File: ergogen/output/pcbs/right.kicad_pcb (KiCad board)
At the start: 2 copper layers, 144.4 x 121 mm, 69 parts

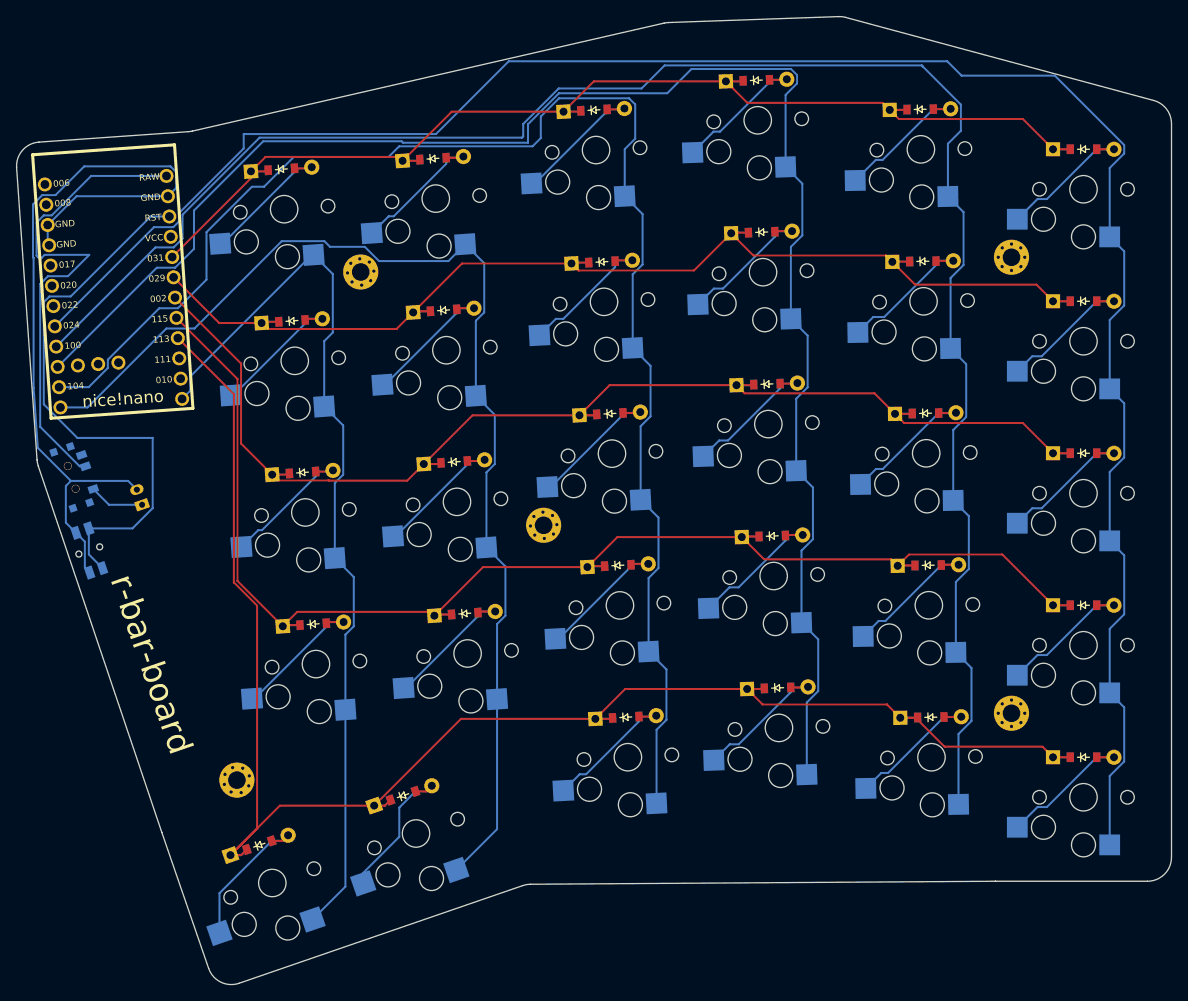
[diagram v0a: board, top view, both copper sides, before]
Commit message: Update keymap
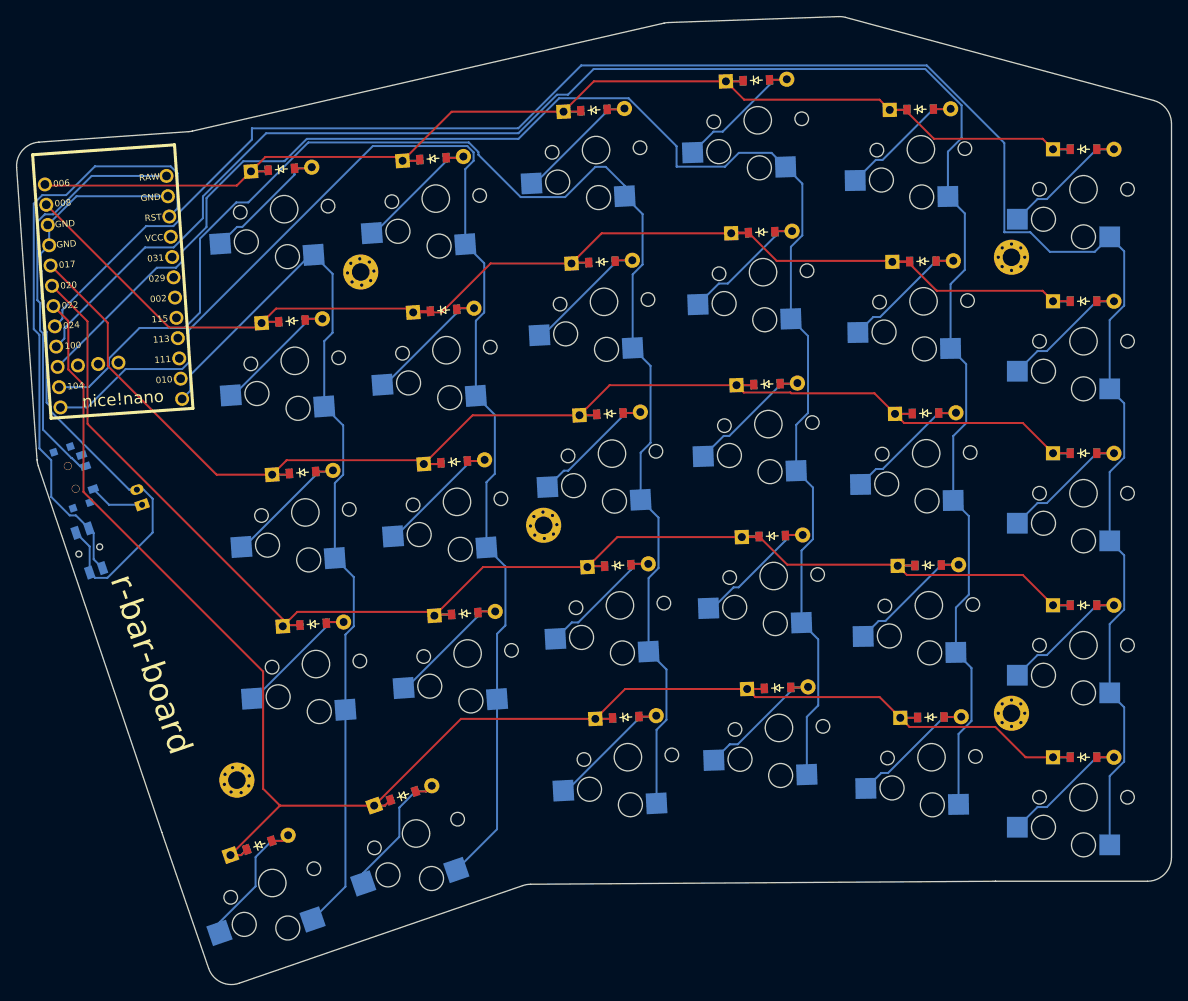
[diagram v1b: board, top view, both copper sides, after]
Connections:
- D1 pad 1: P113 -> P022
- D10 pad 1: P031 -> P006
- D11 pad 1: P113 -> P022
- D12 pad 1: P115 -> P020
- D13 pad 1: P002 -> P017
- D14 pad 1: P029 -> P008
- D15 pad 1: P031 -> P006
- D16 pad 1: P113 -> P022
- D17 pad 1: P115 -> P020
- D18 pad 1: P002 -> P017
- D19 pad 1: P029 -> P008
- D2 pad 1: P115 -> P020
- D20 pad 1: P031 -> P006
- D21 pad 1: P115 -> P020
- D22 pad 1: P002 -> P017
- D23 pad 1: P029 -> P008
- D24 pad 1: P031 -> P006
- D25 pad 1: P115 -> P020
- D26 pad 1: P002 -> P017
- D27 pad 1: P029 -> P008
- D28 pad 1: P031 -> P006
- D29 pad 1: P113 -> P022
- D3 pad 1: P002 -> P017
- D30 pad 1: P113 -> P022
- D4 pad 1: P029 -> P008
- D5 pad 1: P031 -> P006
- D6 pad 1: P113 -> P022
- D7 pad 1: P115 -> P020
- D8 pad 1: P002 -> P017
- D9 pad 1: P029 -> P008
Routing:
- net P022: track 0.00 -> 215.9 mm
- net P113: track 211.8 -> 0.00 mm
- net P020: track 0.00 -> 185.7 mm
- net P115: track 176.4 -> 0.00 mm
- net P017: track 0.00 -> 174.2 mm
- net P008: track 0.00 -> 167.3 mm
- net P006: track 0.00 -> 161.7 mm
- net P002: track 159.9 -> 0.00 mm
- net P031: track 149.9 -> 0.00 mm
- net P029: track 148.1 -> 0.00 mm
- net GND: track 100.7 -> 78.5 mm
- net P106: track 145.7 -> 164.4 mm
- net RAW: track 62.9 -> 52.0 mm
- net P011: track 206.3 -> 196.1 mm
- net P104: track 186.6 -> 177.9 mm
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
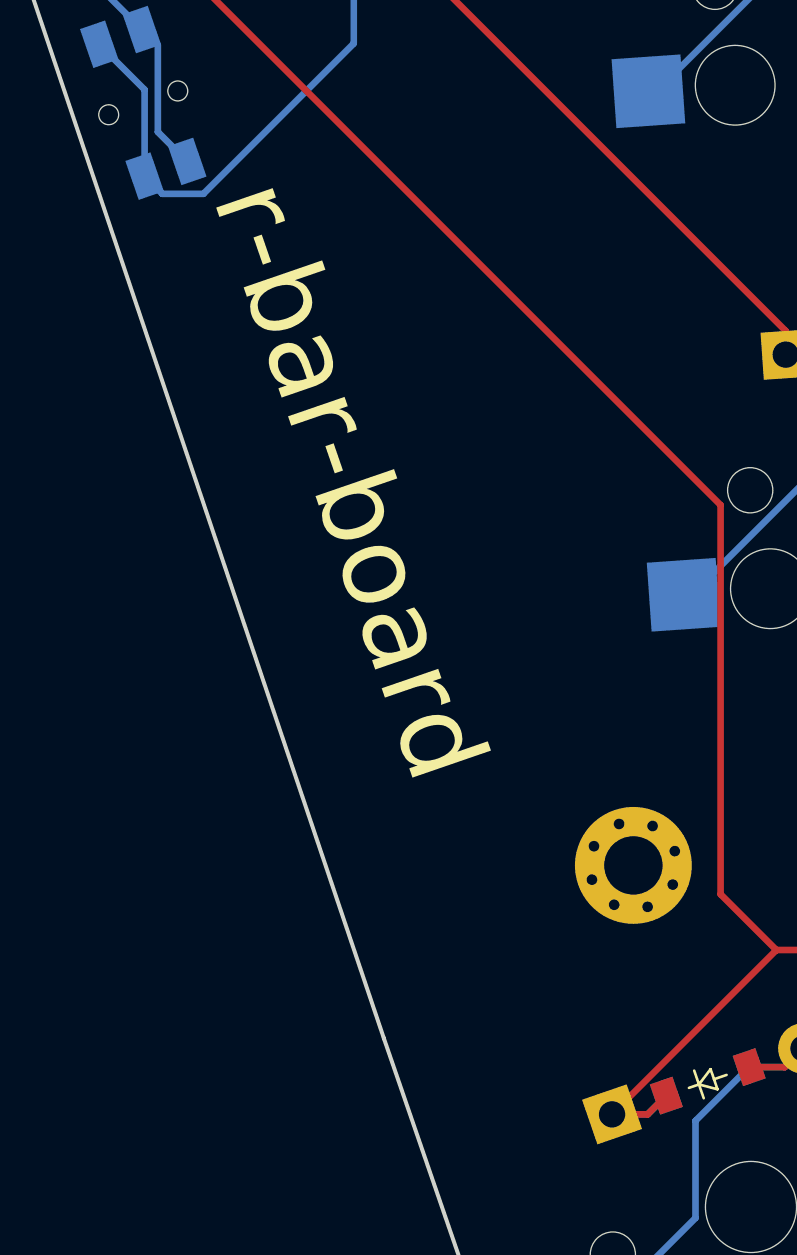
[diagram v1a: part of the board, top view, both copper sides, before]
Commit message: rename with underscores
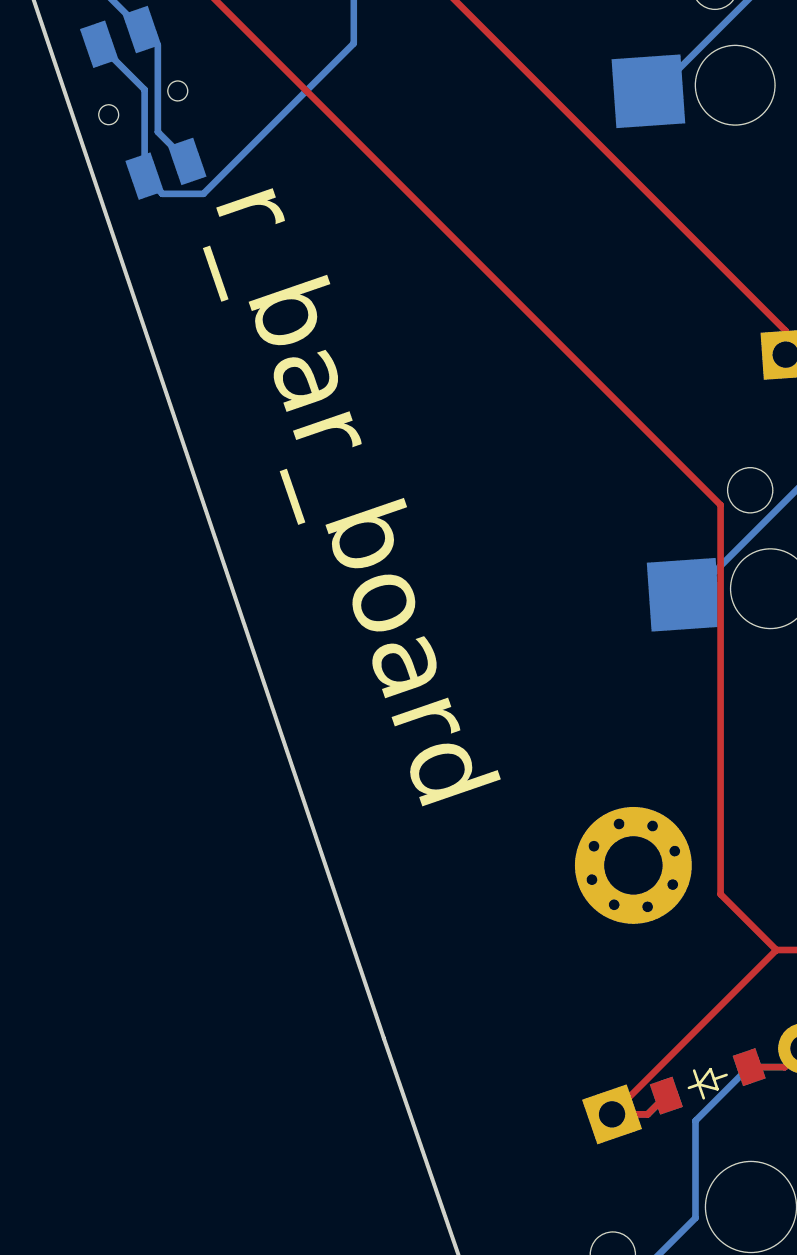
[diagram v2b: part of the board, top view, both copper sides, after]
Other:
- board text added: "r_bar_board"
- board text removed: "r-bar-board"
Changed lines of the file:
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@@
 		(layer "Edge.Cuts")
 	)
-	(gr_text "r-bar-board"
+	(gr_text "r_bar_board"
 		(at 229.4948 172.291066 -71)
 		(layer "F.SilkS")
